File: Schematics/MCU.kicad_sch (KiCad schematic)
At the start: 27 parts, among them J1 Microsemi_FlashPro-JTAG-10, U1 STM32F405RGT6, Y1 8mhz

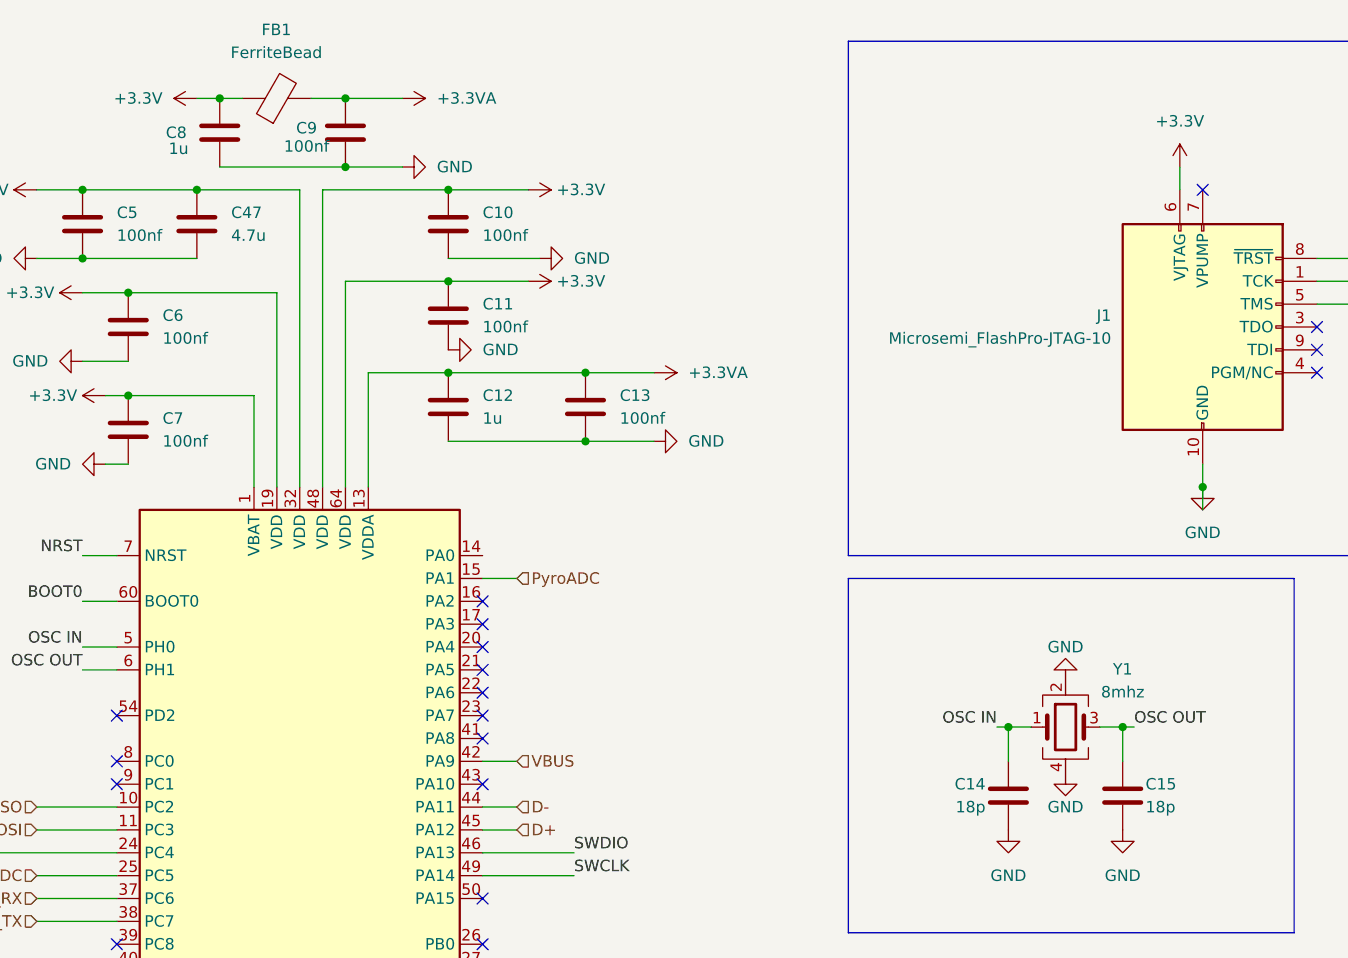
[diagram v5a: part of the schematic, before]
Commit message: added lora correct and organizing sheet pins
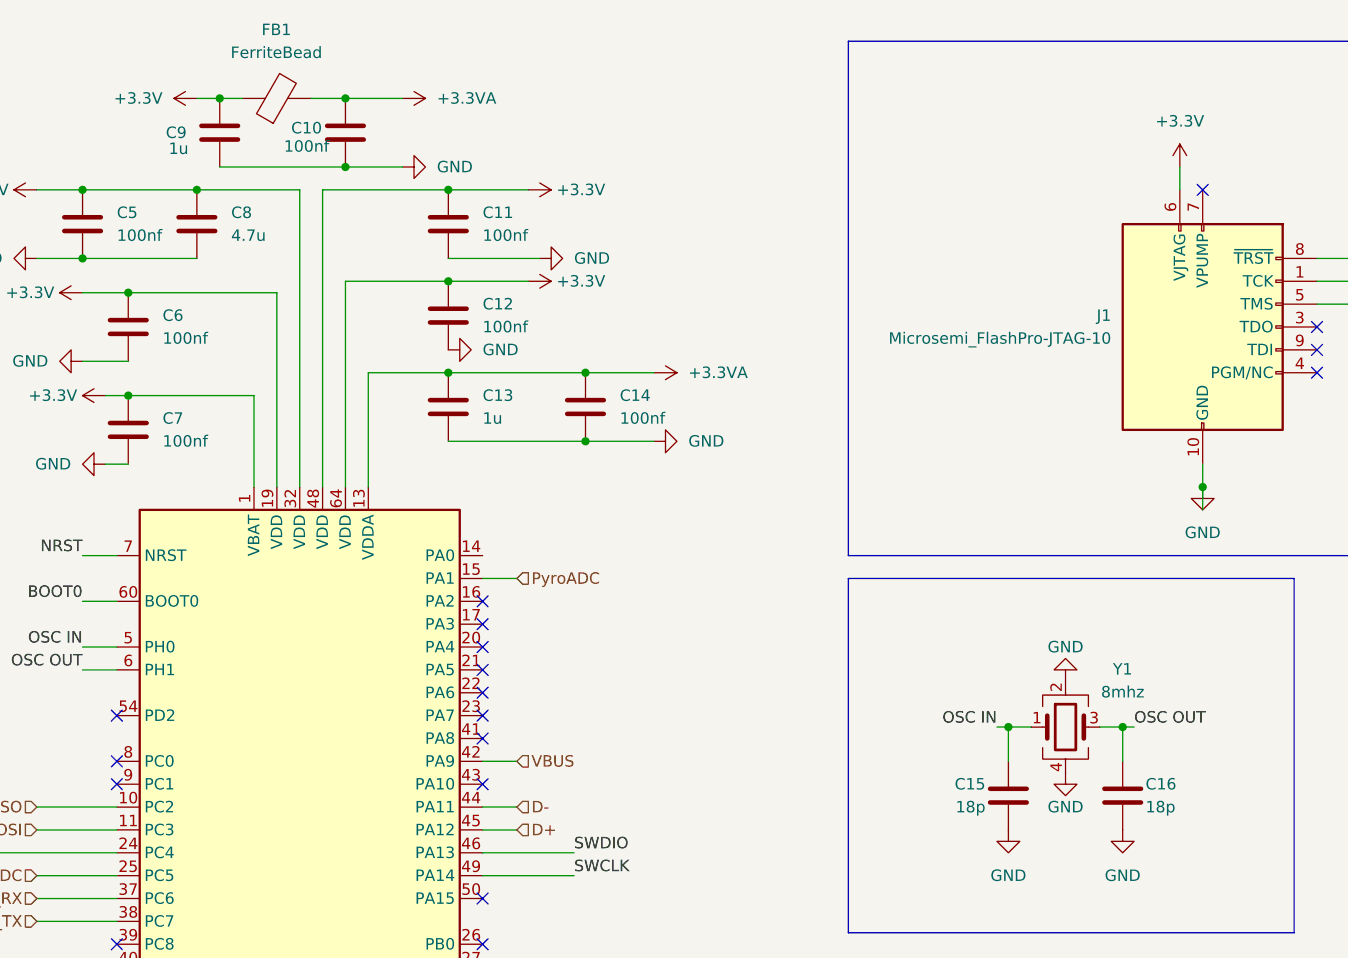
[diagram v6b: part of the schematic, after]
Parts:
- renumbered C9 to C10, C10 to C11, C11 to C12, C12 to C13, C13 to C14, C14 to C15, C15 to C16, C47 to C8, C8 to C9
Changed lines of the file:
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@@
 		(dnp no)
 		(fields_autoplaced yes)
-		(property "Reference" "C12"
+		(property "Reference" "C13"
 			(at 161.29 59.6899 0)
 			(effects
@@
 			(project "flightcomputer2"
 				(path "/6cb3dda3-5fe8-4715-b831-354360aa3199/2415024d-c1fa-457e-8c6b-d01152b96a1d"
-					(reference "C12")
+					(reference "C13")
 					(unit 1)
 				)
@@
 		(dnp no)
 		(fields_autoplaced yes)
-		(property "Reference" "C11"
+		(property "Reference" "C12"
 			(at 161.29 49.5299 0)
 			(effects
@@
 			(project "flightcomputer2"
 				(path "/6cb3dda3-5fe8-4715-b831-354360aa3199/2415024d-c1fa-457e-8c6b-d01152b96a1d"
-					(reference "C11")
+					(reference "C12")
 					(unit 1)
 				)
@@
 		(dnp no)
 		(fields_autoplaced yes)
-		(property "Reference" "C10"
+		(property "Reference" "C11"
 			(at 161.29 39.3699 0)
 			(effects
@@
 			(project "flightcomputer2"
 				(path "/6cb3dda3-5fe8-4715-b831-354360aa3199/2415024d-c1fa-457e-8c6b-d01152b96a1d"
-					(reference "C10")
+					(reference "C11")
 					(unit 1)
 				)
@@
 		(dnp no)
 		(fields_autoplaced yes)
-		(property "Reference" "C47"
+		(property "Reference" "C8"
 			(at 133.35 39.3699 0)
 			(effects
@@
 			(project "flightcomputer2"
 				(path "/6cb3dda3-5fe8-4715-b831-354360aa3199/2415024d-c1fa-457e-8c6b-d01152b96a1d"
-					(reference "C47")
+					(reference "C8")
 					(unit 1)
 				)
@@
 		(on_board yes)
 		(dnp no)
-		(property "Reference" "C9"
+		(property "Reference" "C10"
 			(at 141.732 29.972 0)
 			(effects
@@
 			(project "flightcomputer2"
 				(path "/6cb3dda3-5fe8-4715-b831-354360aa3199/2415024d-c1fa-457e-8c6b-d01152b96a1d"
-					(reference "C9")
+					(reference "C10")
 					(unit 1)
 				)
@@
 		(dnp no)
 		(fields_autoplaced yes)
-		(property "Reference" "C13"
+		(property "Reference" "C14"
 			(at 176.53 59.6899 0)
 			(effects
@@
 			(project "flightcomputer2"
 				(path "/6cb3dda3-5fe8-4715-b831-354360aa3199/2415024d-c1fa-457e-8c6b-d01152b96a1d"
-					(reference "C13")
+					(reference "C14")
 					(unit 1)
 				)
@@
 		(on_board yes)
 		(dnp no)
-		(property "Reference" "C8"
+		(property "Reference" "C9"
 			(at 127.254 30.48 0)
 			(effects
@@
 			(project "flightcomputer2"
 				(path "/6cb3dda3-5fe8-4715-b831-354360aa3199/2415024d-c1fa-457e-8c6b-d01152b96a1d"
-					(reference "C8")
+					(reference "C9")
 					(unit 1)
 				)
@@
 		(on_board yes)
 		(dnp no)
-		(property "Reference" "C15"
+		(property "Reference" "C16"
 			(at 234.95 102.87 0)
 			(effects
@@
 			(project "flightcomputer2"
 				(path "/6cb3dda3-5fe8-4715-b831-354360aa3199/2415024d-c1fa-457e-8c6b-d01152b96a1d"
-					(reference "C15")
+					(reference "C16")
 					(unit 1)
 				)
@@
 		(on_board yes)
 		(dnp no)
-		(property "Reference" "C14"
+		(property "Reference" "C15"
 			(at 217.17 102.87 0)
 			(effects
@@
 			(project "flightcomputer2"
 				(path "/6cb3dda3-5fe8-4715-b831-354360aa3199/2415024d-c1fa-457e-8c6b-d01152b96a1d"
-					(reference "C14")
+					(reference "C15")
 					(unit 1)
 				)

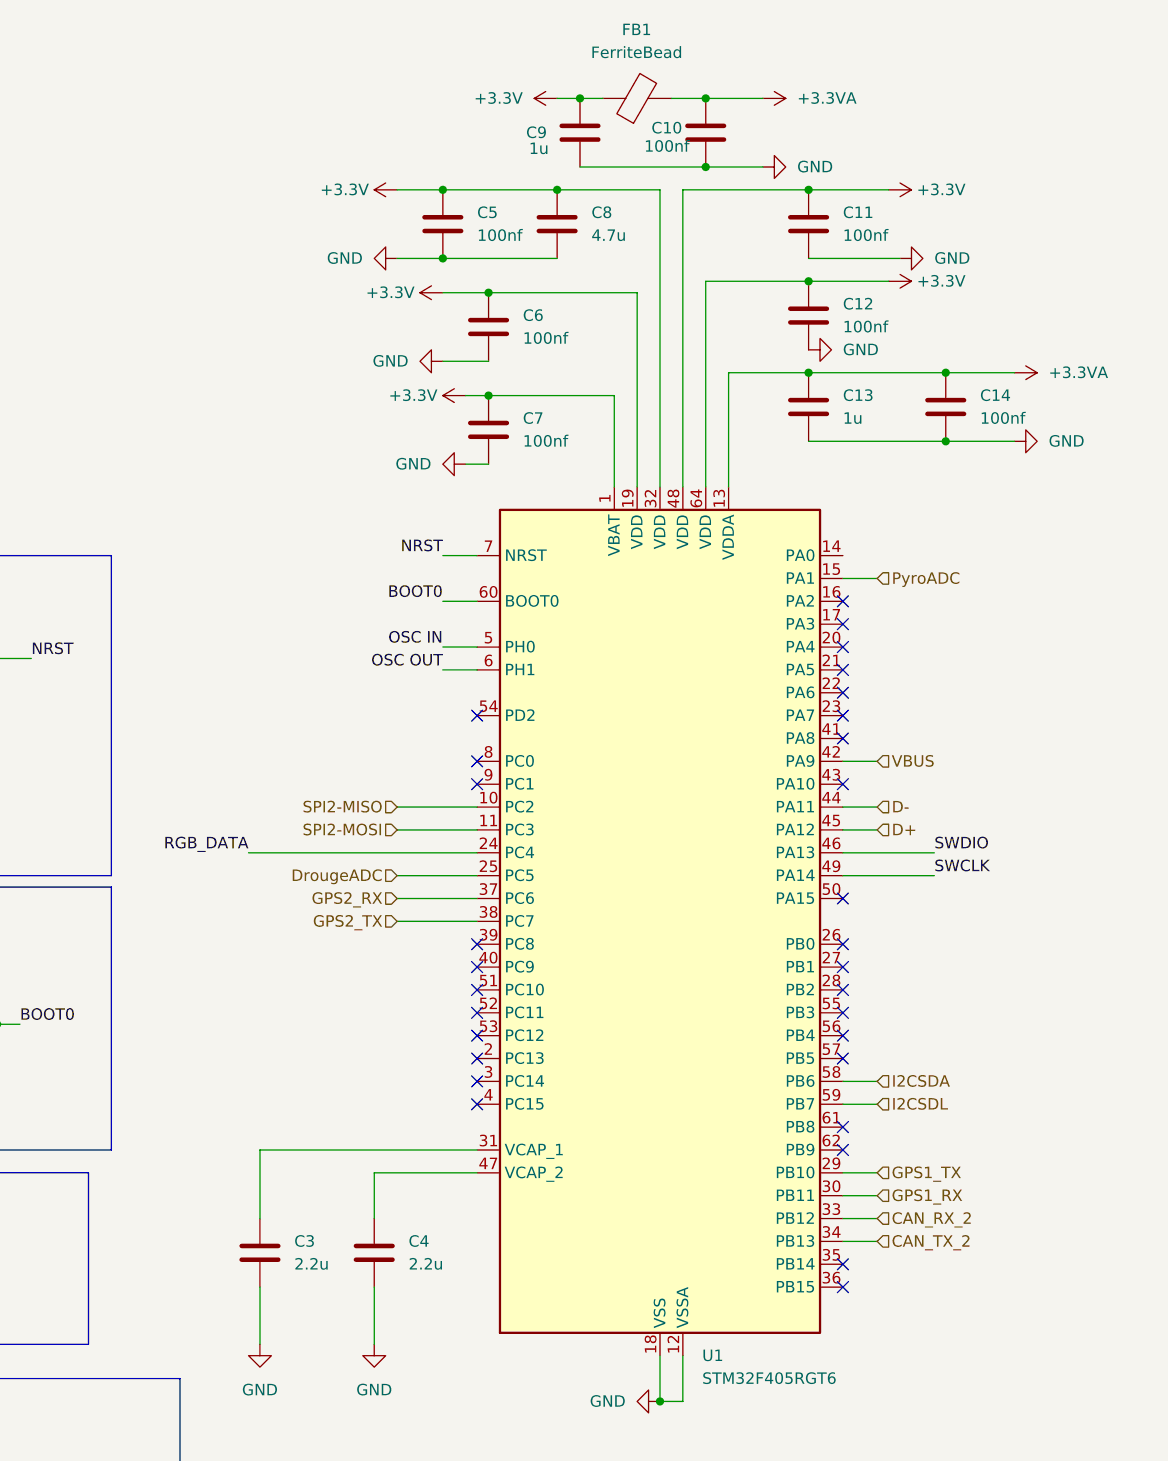
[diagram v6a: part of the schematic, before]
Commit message: finished pin assignments and ran ERC all good ready for layout
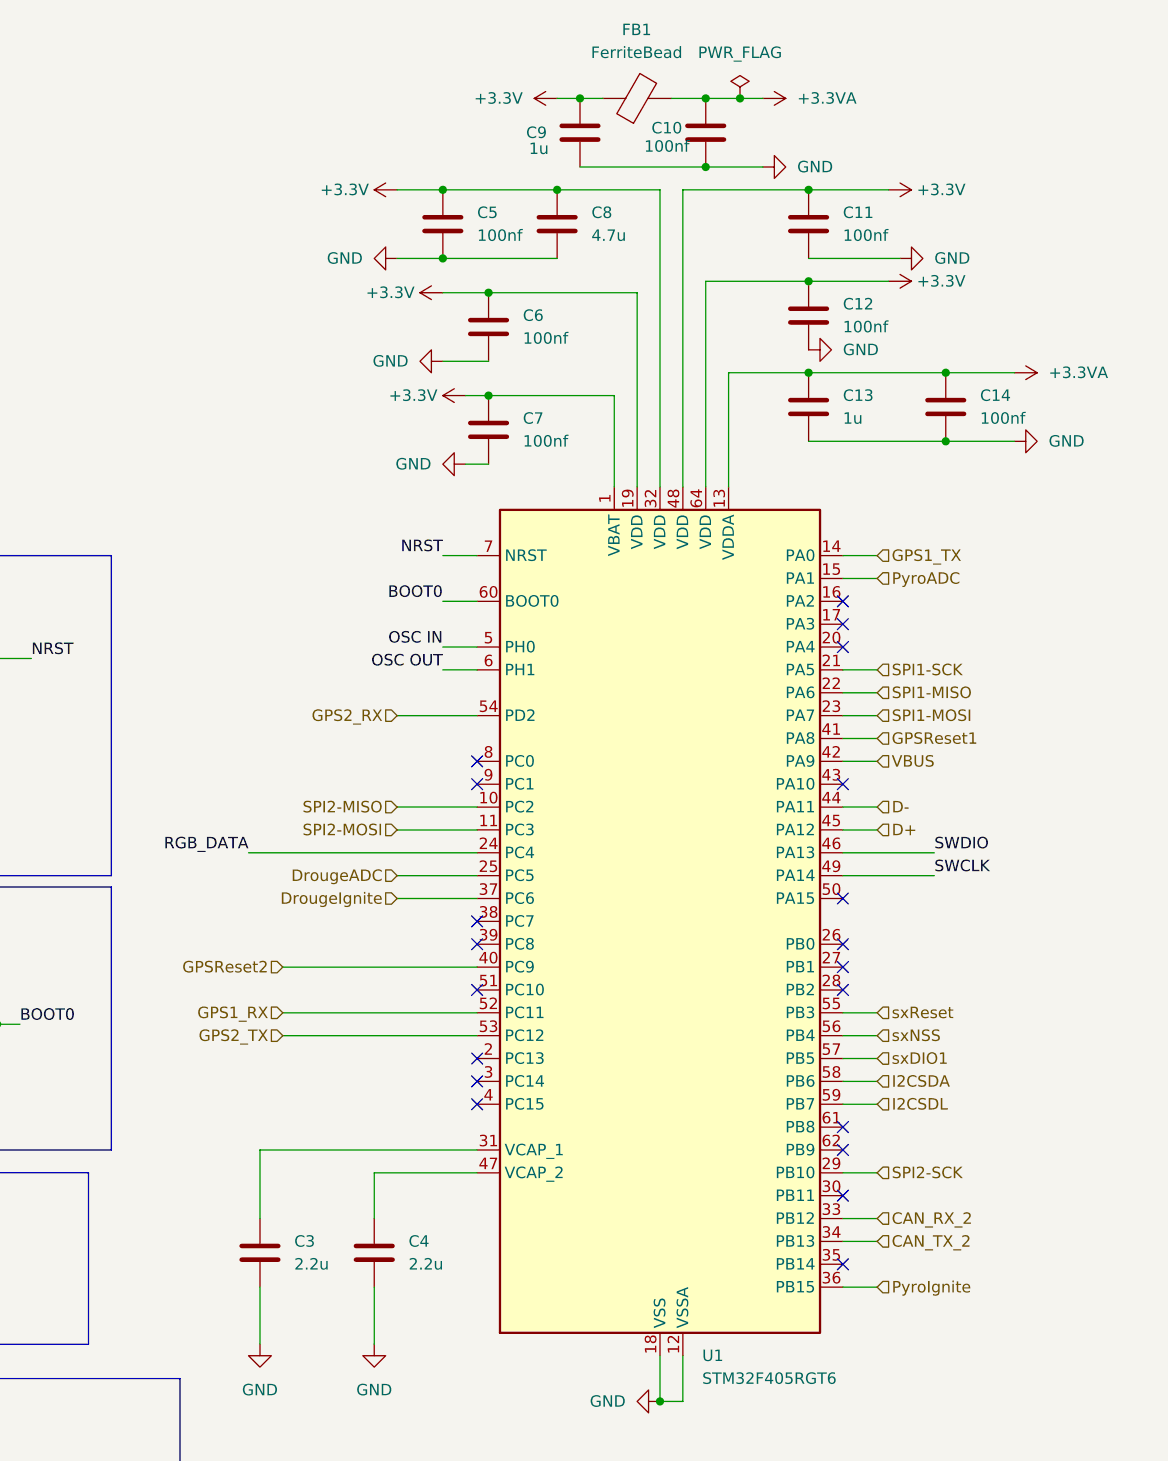
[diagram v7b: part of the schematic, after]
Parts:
- C15, C16: footprint Capacitor_SMD:C_0603_1608Metric_Pad1.08x0.95mm_HandSolder -> Capacitor_SMD:C_0805_2012Metric_Pad1.18x1.45mm_HandSolder; LCSC Part C1647 -> C170109
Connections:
- net GPS1_RX: now also U1.52 (PC11); no longer U1.30 (PB11)
- net GPS1_TX: now also U1.14 (PA0); no longer U1.29 (PB10)
- net GPS2_RX: now also U1.54 (PD2); no longer U1.37 (PC6)
- net GPS2_TX: now also U1.53 (PC12); no longer U1.38 (PC7)
- net SPI1-SCK: now reaches U1.21 (PA5)
- net SPI1-MISO: now reaches U1.22 (PA6)
- net SPI1-MOSI: now reaches U1.23 (PA7)
- net PyroIgnite: now reaches U1.36 (PB15)
- net GPSReset2: now reaches U1.40 (PC9)
- net GPSReset1: now reaches U1.41 (PA8)
- net sxReset: now reaches U1.55 (PB3)
- net sxNSS: now reaches U1.56 (PB4)
- net sxDIO1: now reaches U1.57 (PB5)
- new net DrougeIgnite: U1.37 (PC6)
- new net SPI2-SCK: U1.29 (PB10)
- no-connect marks 39 -> 29

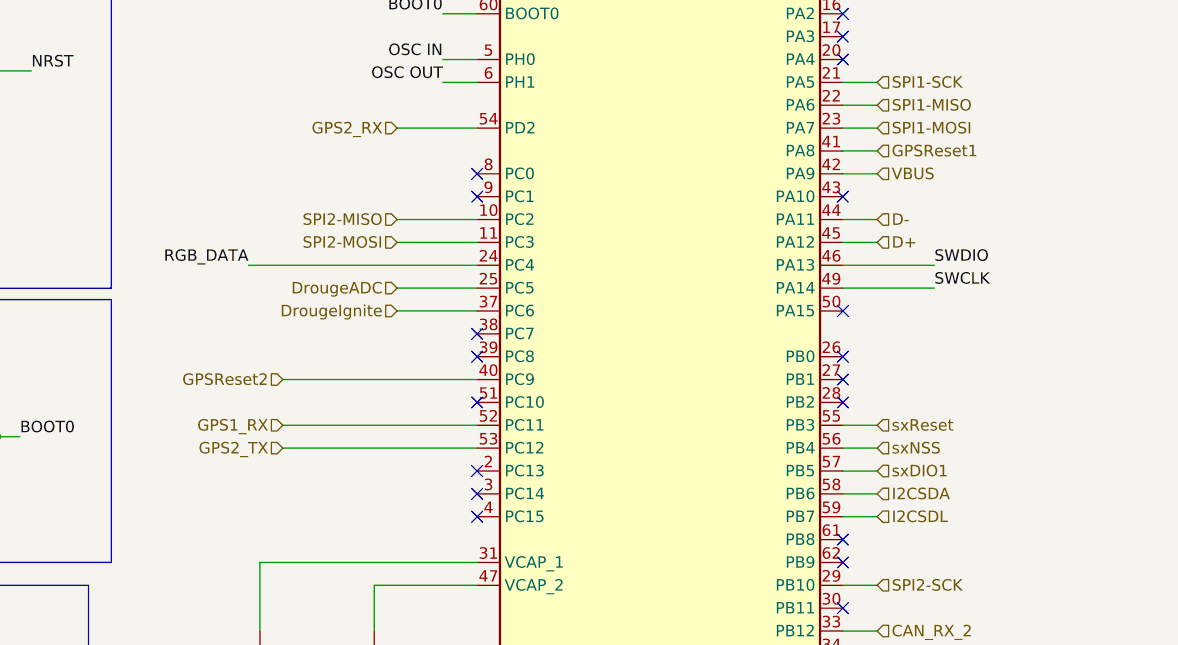
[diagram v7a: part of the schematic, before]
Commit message: Added Flash memory
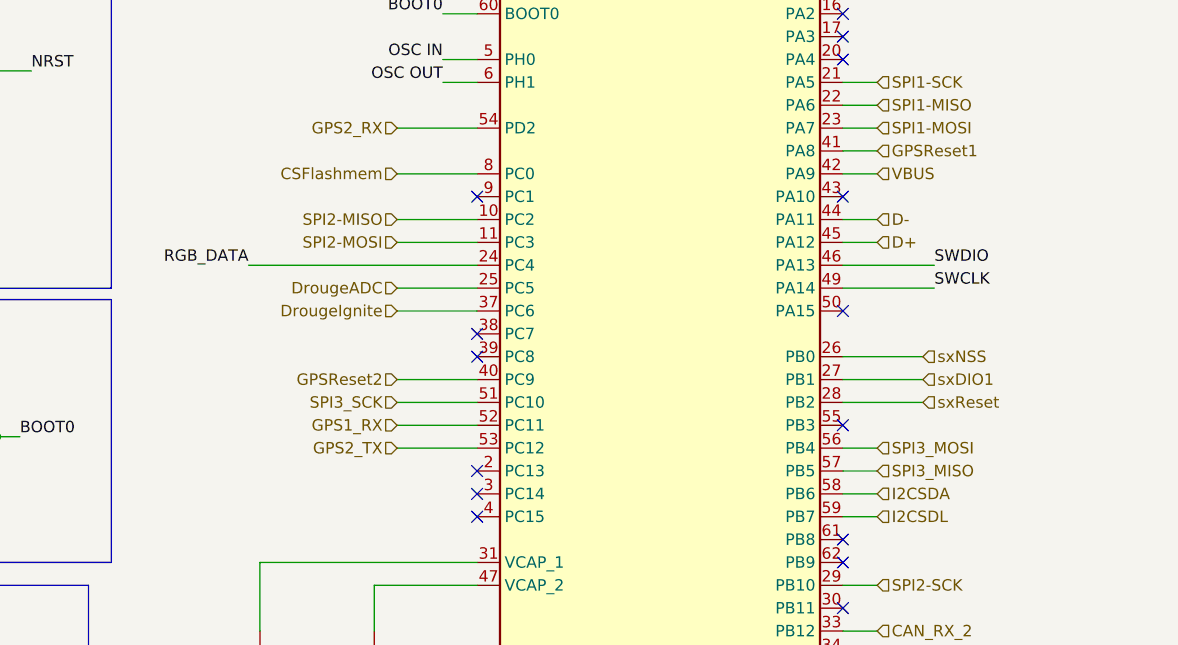
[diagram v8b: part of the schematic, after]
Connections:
- net sxDIO1: now also U1.27 (PB1); no longer U1.57 (PB5)
- net sxNSS: now also U1.26 (PB0); no longer U1.56 (PB4)
- net sxReset: now also U1.28 (PB2); no longer U1.55 (PB3)
- net SPI3_SCK: now reaches U1.51 (PC10)
- net CSFlashmem: now reaches U1.8 (PC0)
- new net SPI3_MISO: U1.57 (PB5)
- new net SPI3_MOSI: U1.56 (PB4)
- no-connect marks 29 -> 25
